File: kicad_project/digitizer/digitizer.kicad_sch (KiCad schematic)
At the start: 0 parts

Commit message: finished schematic symbol for the LPC1813JBD144, and connected it to the LQFP144 footprint! Placed it into the schematic
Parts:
- added U?: LPC1813JBD144, 495-project-library:LQFP-144_20x20mm_P0.5mm, symbol 495-project-library:LPC1813JBD144
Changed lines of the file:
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@@
 (kicad_sch (version 20211123) (generator eeschema)
   (paper "A4")
+  (symbol (lib_id "495-project-library:LPC1813JBD144") (at 240.03 142.24 90) (unit 1)
+    (in_bom yes) (on_board yes) (fields_autoplaced)
+    (property "Reference" "U?" (id 0) (at 248.92 22.1105 90))
+    (property "Value" "LPC1813JBD144" (id 1) (at 248.92 24.6505 90))
+    (property "Footprint" "495-project-library:LQFP-144_20x20mm_P0.5mm" (id 2) (at 99.695 67.31 0)
+      (effects (font (size 1.27 1.27)) hide)
+    )
+    (property "Datasheet" "" (id 3) (at 99.695 67.31 0)
+      (effects (font (size 1.27 1.27)) hide)
+    )
+    (pin "1")
+    (pin "10")
+    (pin "100")
+    (pin "101")
+    (pin "102")
+    (pin "103")
+    (pin "104")
+    (pin "105")
+    (pin "106")
+    (pin "107")
+    (pin "108")
+    (pin "109")
+    (pin "11")
+    (pin "110")
+    (pin "111")
+    (pin "112")
+    (pin "113")
+    (pin "114")
+    (pin "115")
+    (pin "116")
+    (pin "117")
+    (pin "118")
+    (pin "119")
+    (pin "12")
+    (pin "120")
+    (pin "121")
+    (pin "122")
+    (pin "123")
+    (pin "124")
+    (pin "125")
+    (pin "126")
+    (pin "127")
+    (pin "128")
+    (pin "129")
+    (pin "13")
+    (pin "130")
+    (pin "131")
+    (pin "132")
+    (pin "133")
+    (pin "134")
+    (pin "135")
+    (pin "136")
+    (pin "137")
+    (pin "138")
+    (pin "139")
+    (pin "14")
+    (pin "140")
+    (pin "141")
+    (pin "142")
+    (pin "143")
+    (pin "144")
+    (pin "15")
+    (pin "16")
+    (pin "17")
+    (pin "18")
+    (pin "19")
+    (pin "2")
+    (pin "20")
+    (pin "21")
+    (pin "22")
+    (pin "23")
+    (pin "24")
+    (pin "25")
+    (pin "26")
+    (pin "27")
+    (pin "28")
+    (pin "29")
+    (pin "3")
+    (pin "30")
+    (pin "31")
+    (pin "32")
+    (pin "33")
+    (pin "34")
+    (pin "35")
+    (pin "36")
+    (pin "37")
+    (pin "38")
+    (pin "39")
+    (pin "4")
+    (pin "40")
+    (pin "41")
+    (pin "42")
+    (pin "43")
+    (pin "44")
+    (pin "45")
+    (pin "46")
+    (pin "47")
+    (pin "48")
+    (pin "49")
+    (pin "5")
+    (pin "50")
+    (pin "51")
+    (pin "52")
+    (pin "53")
+    (pin "54")
+    (pin "55")
+    (pin "56")
+    (pin "57")
+    (pin "58")
+    (pin "59")
+    (pin "6")
+    (pin "60")
+    (pin "61")
+    (pin "62")
+    (pin "63")
+    (pin "64")
+    (pin "65")
+    (pin "66")
+    (pin "67")
+    (pin "68")
+    (pin "69")
+    (pin "7")
+    (pin "70")
+    (pin "71")
+    (pin "72")
+    (pin "73")
+    (pin "74")
+    (pin "75")
+    (pin "76")
+    (pin "77")
+    (pin "78")
+    (pin "79")
+    (pin "8")
+    (pin "80")
+    (pin "81")
+    (pin "82")
+    (pin "83")
+    (pin "84")
+    (pin "85")
+    (pin "86")
+    (pin "87")
+    (pin "88")
+    (pin "89")
+    (pin "9")
+    (pin "90")
+    (pin "91")
+    (pin "92")
+    (pin "93")
+    (pin "94")
+    (pin "95")
+    (pin "96")
+    (pin "97")
+    (pin "98")
+    (pin "99")
+  )
   (sheet_instances
     (path "/" (page "1"))
   )
+  (symbol_instances
+    (path "/52eeadc6-ab00-4433-9657-3deb36d0623b"
+      (reference "U?") (unit 1) (value "LPC1813JBD144") (footprint "495-project-library:LQFP-144_20x20mm_P0.5mm")
+    )
+  )
 )

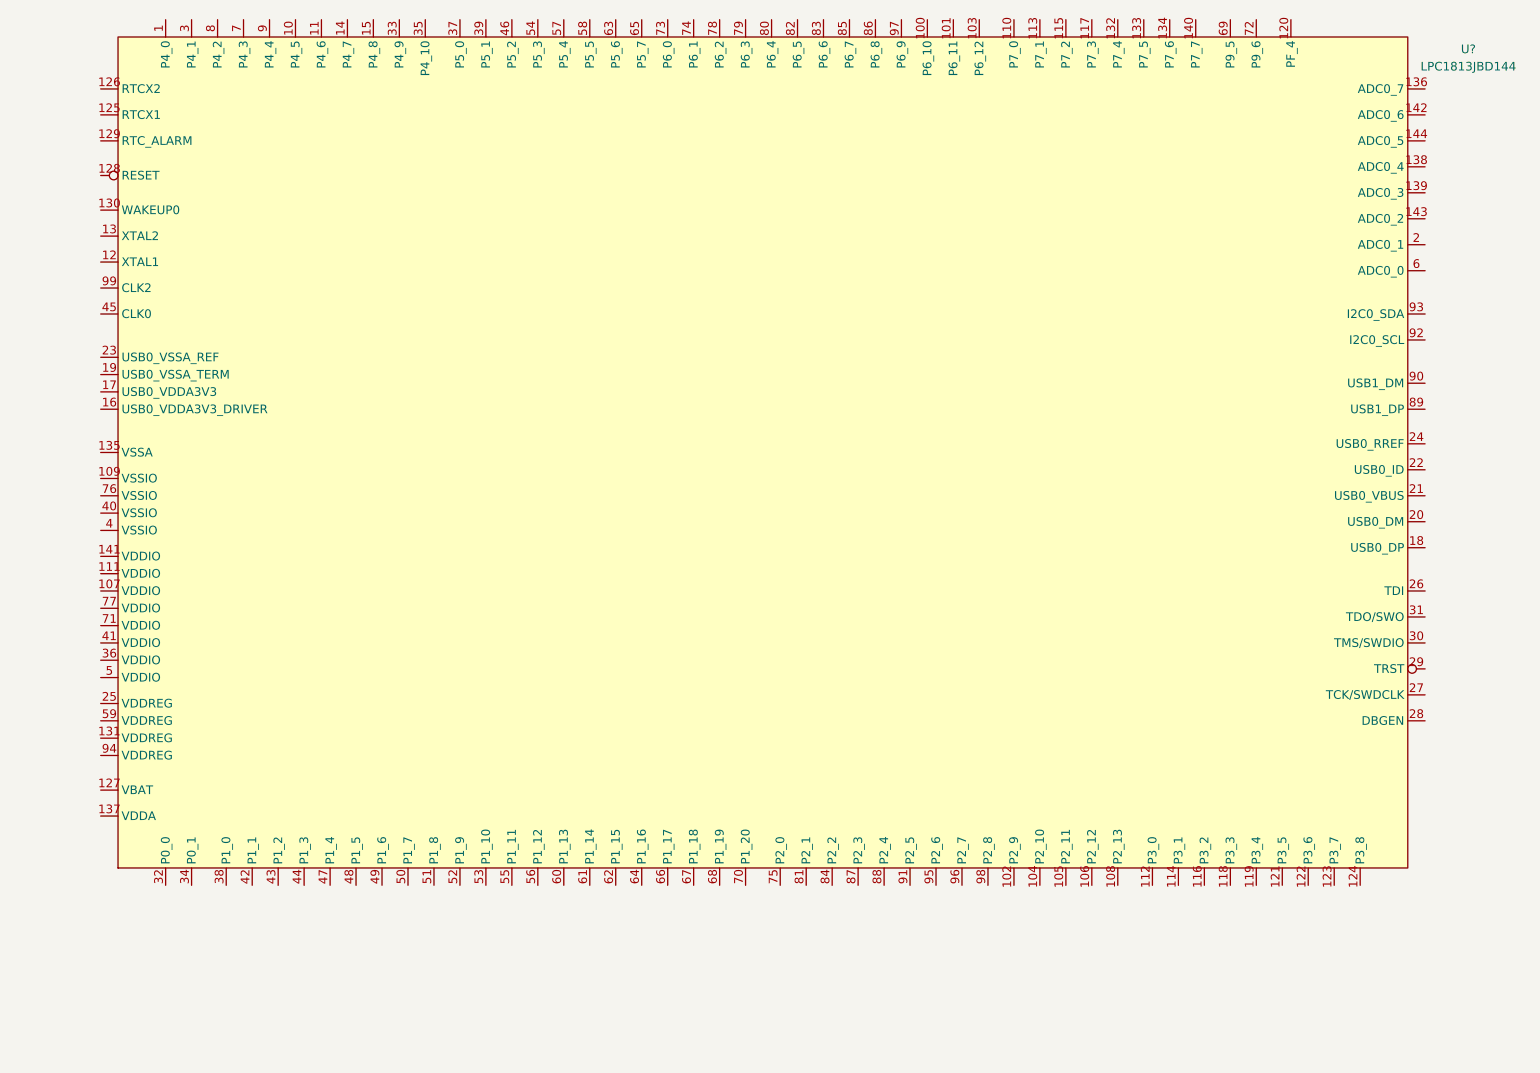
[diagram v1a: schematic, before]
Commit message: divided schematic up into 3 sheets, and placed the corresponding components within them. Have not connected anything or match the correct connectors to the proper footprints yet
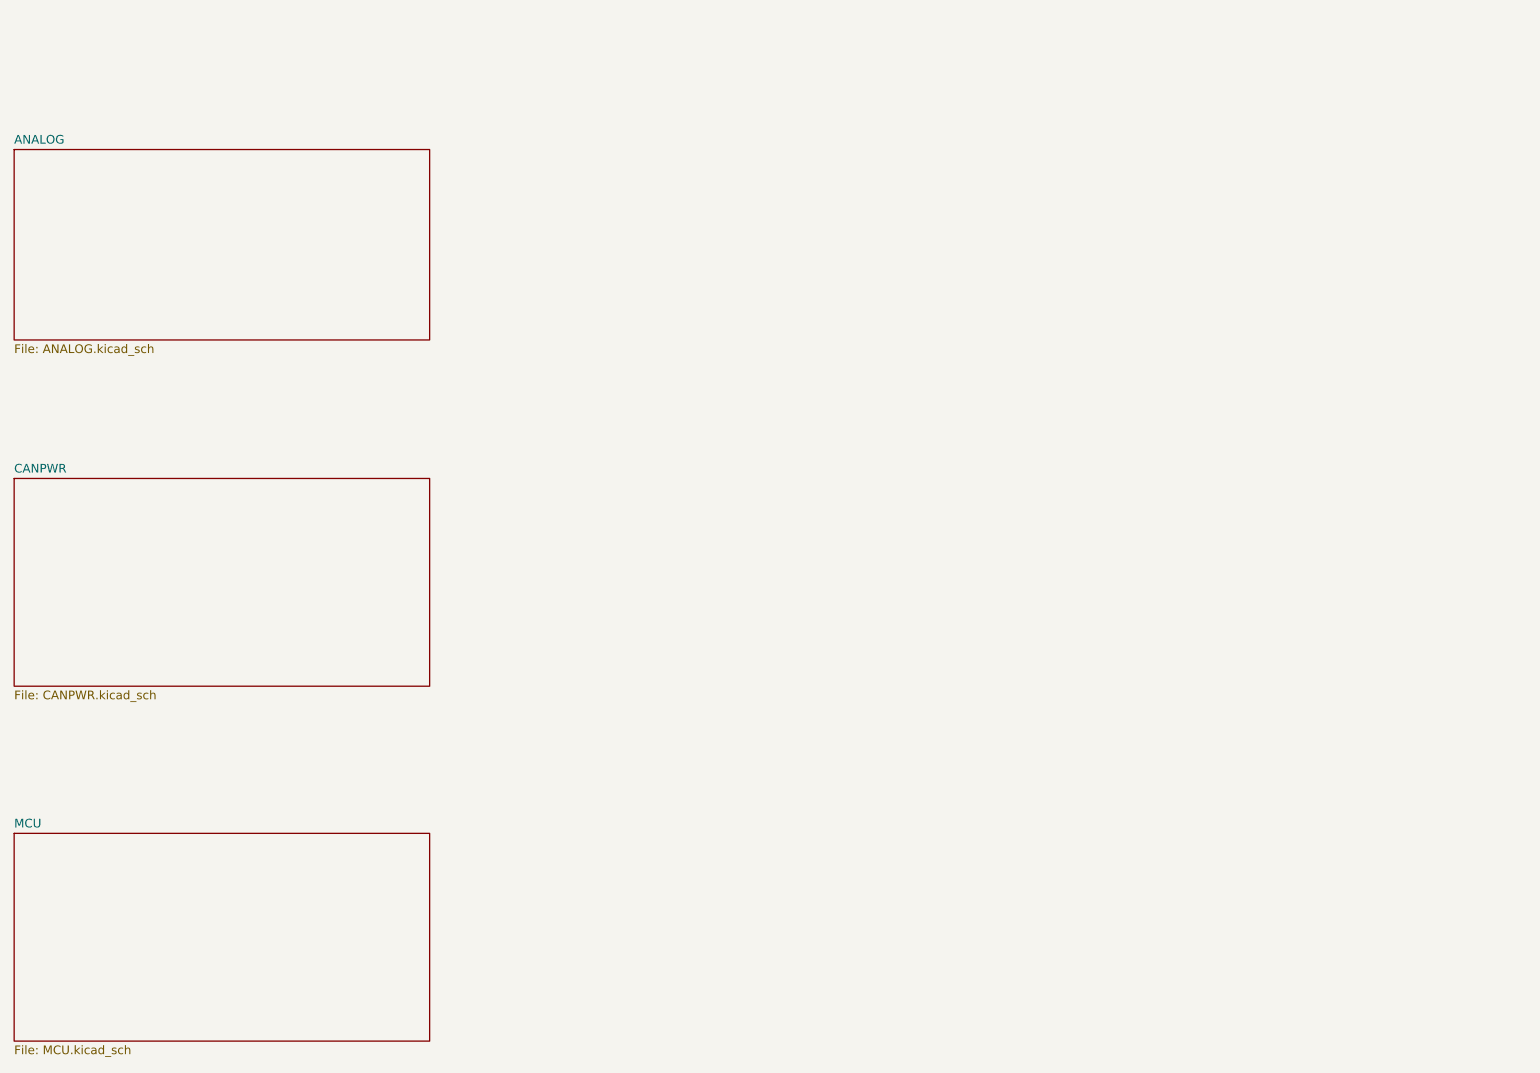
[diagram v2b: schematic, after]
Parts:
- removed U?: LPC1813JBD144, 495-project-library:LQFP-144_20x20mm_P0.5mm, symbol 495-project-library:LPC1813JBD144
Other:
- added sheet ANALOG (ANALOG.kicad_sch)
- added sheet CANPWR (CANPWR.kicad_sch)
- added sheet MCU (MCU.kicad_sch)
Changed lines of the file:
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@@
 (kicad_sch (version 20211123) (generator eeschema)
   (paper "A4")
-  (symbol (lib_id "495-project-library:LPC1813JBD144") (at 240.03 142.24 90) (unit 1)
-    (in_bom yes) (on_board yes) (fields_autoplaced)
-    (property "Reference" "U?" (id 0) (at 248.92 22.1105 90))
-    (property "Value" "LPC1813JBD144" (id 1) (at 248.92 24.6505 90))
-    (property "Footprint" "495-project-library:LQFP-144_20x20mm_P0.5mm" (id 2) (at 99.695 67.31 0)
-      (effects (font (size 1.27 1.27)) hide)
+  (sheet (at 35.56 137.16) (size 60.96 30.48) (fields_autoplaced)
+    (stroke (width 0.1524) (type solid) (color 0 0 0 0))
+    (fill (color 0 0 0 0.0000))
+    (property "Sheet name" "MCU" (id 0) (at 35.56 136.4484 0)
+      (effects (font (size 1.27 1.27)) (justify left bottom))
     )
-    (property "Datasheet" "" (id 3) (at 99.695 67.31 0)
-      (effects (font (size 1.27 1.27)) hide)
+    (property "Sheet file" "MCU.kicad_sch" (id 1) (at 35.56 168.2246 0)
+      (effects (font (size 1.27 1.27)) (justify left top))
     )
-    (pin "1")
-    (pin "10")
-    (pin "100")
-    (pin "101")
-    (pin "102")
-    (pin "103")
-    (pin "104")
-    (pin "105")
-    (pin "106")
-    (pin "107")
-    (pin "108")
-    (pin "109")
-    (pin "11")
-    (pin "110")
-    (pin "111")
-    (pin "112")
-    (pin "113")
-    (pin "114")
-    (pin "115")
-    (pin "116")
-    (pin "117")
-    (pin "118")
-    (pin "119")
-    (pin "12")
-    (pin "120")
-    (pin "121")
-    (pin "122")
-    (pin "123")
-    (pin "124")
-    (pin "125")
-    (pin "126")
-    (pin "127")
-    (pin "128")
-    (pin "129")
-    (pin "13")
-    (pin "130")
-    (pin "131")
-    (pin "132")
-    (pin "133")
-    (pin "134")
-    (pin "135")
-    (pin "136")
-    (pin "137")
-    (pin "138")
-    (pin "139")
-    (pin "14")
-    (pin "140")
-    (pin "141")
-    (pin "142")
-    (pin "143")
-    (pin "144")
-    (pin "15")
-    (pin "16")
-    (pin "17")
-    (pin "18")
-    (pin "19")
-    (pin "2")
-    (pin "20")
-    (pin "21")
-    (pin "22")
-    (pin "23")
-    (pin "24")
-    (pin "25")
-    (pin "26")
-    (pin "27")
-    (pin "28")
-    (pin "29")
-    (pin "3")
-    (pin "30")
-    (pin "31")
-    (pin "32")
-    (pin "33")
-    (pin "34")
-    (pin "35")
-    (pin "36")
-    (pin "37")
-    (pin "38")
-    (pin "39")
-    (pin "4")
-    (pin "40")
-    (pin "41")
-    (pin "42")
-    (pin "43")
-    (pin "44")
-    (pin "45")
-    (pin "46")
-    (pin "47")
-    (pin "48")
-    (pin "49")
-    (pin "5")
-    (pin "50")
-    (pin "51")
-    (pin "52")
-    (pin "53")
-    (pin "54")
-    (pin "55")
-    (pin "56")
-    (pin "57")
-    (pin "58")
-    (pin "59")
-    (pin "6")
-    (pin "60")
-    (pin "61")
-    (pin "62")
-    (pin "63")
-    (pin "64")
-    (pin "65")
-    (pin "66")
-    (pin "67")
-    (pin "68")
-    (pin "69")
-    (pin "7")
-    (pin "70")
-    (pin "71")
-    (pin "72")
-    (pin "73")
-    (pin "74")
-    (pin "75")
-    (pin "76")
-    (pin "77")
-    (pin "78")
-    (pin "79")
-    (pin "8")
-    (pin "80")
-    (pin "81")
-    (pin "82")
-    (pin "83")
-    (pin "84")
-    (pin "85")
-    (pin "86")
-    (pin "87")
-    (pin "88")
-    (pin "89")
-    (pin "9")
-    (pin "90")
-    (pin "91")
-    (pin "92")
-    (pin "93")
-    (pin "94")
-    (pin "95")
-    (pin "96")
-    (pin "97")
-    (pin "98")
-    (pin "99")
+  )
+  (sheet (at 35.56 36.83) (size 60.96 27.94) (fields_autoplaced)
+    (stroke (width 0.1524) (type solid) (color 0 0 0 0))
+    (fill (color 0 0 0 0.0000))
+    (property "Sheet name" "ANALOG" (id 0) (at 35.56 36.1184 0)
+      (effects (font (size 1.27 1.27)) (justify left bottom))
+    )
+    (property "Sheet file" "ANALOG.kicad_sch" (id 1) (at 35.56 65.3546 0)
+      (effects (font (size 1.27 1.27)) (justify left top))
+    )
+  )
+  (sheet (at 35.56 85.09) (size 60.96 30.48) (fields_autoplaced)
+    (stroke (width 0.1524) (type solid) (color 0 0 0 0))
+    (fill (color 0 0 0 0.0000))
+    (property "Sheet name" "CANPWR" (id 0) (at 35.56 84.3784 0)
+      (effects (font (size 1.27 1.27)) (justify left bottom))
+    )
+    (property "Sheet file" "CANPWR.kicad_sch" (id 1) (at 35.56 116.1546 0)
+      (effects (font (size 1.27 1.27)) (justify left top))
+    )
   )
   (sheet_instances
     (path "/" (page "1"))
+    (path "/e2c8983e-9459-4573-b339-1f4298bf65be" (page "3"))
+    (path "/8e4bebbd-b918-44d5-8394-c191f4e972d3" (page "4"))
+    (path "/59857acb-489d-4d58-af14-88362a204248" (page "4"))
   )
   (symbol_instances
-    (path "/52eeadc6-ab00-4433-9657-3deb36d0623b"
+    (path "/e2c8983e-9459-4573-b339-1f4298bf65be/3e420adc-3f3e-4ad7-b9e2-5ff4f66087d2"
+      (reference "IC?") (unit 1) (value "MAX6035AAUR50+T") (footprint "SOT95P237X112-3N")
+    )
+    (path "/59857acb-489d-4d58-af14-88362a204248/435a8de2-d92d-404b-a204-1b8d6d9f362a"
+      (reference "IC?") (unit 1) (value "MAX3059ASA+T") (footprint "SOIC127P600X175-8N")
+    )
+    (path "/8e4bebbd-b918-44d5-8394-c191f4e972d3/5b20aef5-6bd8-47f7-86aa-1a7e55b9d139"
+      (reference "IC?") (unit 1) (value "ADS1234IPWR") (footprint "SOP65P640X120-28N")
+    )
+    (path "/59857acb-489d-4d58-af14-88362a204248/84e94675-43a7-4212-9e62-0f780abfd06b"
+      (reference "IC?") (unit 1) (value "MAX3059ASA+T") (footprint "SOIC127P600X175-8N")
+    )
+    (path "/e2c8983e-9459-4573-b339-1f4298bf65be/932b1a92-f5d2-47d1-b1f0-1f4180d05597"
+      (reference "IC?") (unit 1) (value "MAX6043BAUT33+T") (footprint "SOT95P280X145-6N")
+    )
+    (path "/8e4bebbd-b918-44d5-8394-c191f4e972d3/2d66c624-9968-40cd-9f77-7c3c08aebcc4"
+      (reference "J?") (unit 1) (value "Conn_01x04_Shielded") (footprint "")
+    )
+    (path "/59857acb-489d-4d58-af14-88362a204248/4fddafb8-a80f-479c-bb72-09844a9cb710"
+      (reference "J?") (unit 1) (value "Conn_02x05_Odd_Even") (footprint "")
+    )
+    (path "/8e4bebbd-b918-44d5-8394-c191f4e972d3/5869e0e4-d092-4d61-b78f-cfb0c7b24996"
+      (reference "J?") (unit 1) (value "Conn_01x04_Shielded") (footprint "")
+    )
+    (path "/8e4bebbd-b918-44d5-8394-c191f4e972d3/6a83202a-13be-499d-b6b6-ad5d3d904d4f"
+      (reference "J?") (unit 1) (value "Conn_01x04_Shielded") (footprint "")
+    )
+    (path "/e2c8983e-9459-4573-b339-1f4298bf65be/b0aa02d7-c635-47f3-95a7-51b0d8bfd025"
+      (reference "J?") (unit 1) (value "Conn_02x02_Top_Bottom") (footprint "")
+    )
+    (path "/e2c8983e-9459-4573-b339-1f4298bf65be/cb564194-f3a5-43dc-92c5-a4986c563991"
+      (reference "J?") (unit 1) (value "Conn_02x02_Top_Bottom") (footprint "")
+    )
+    (path "/59857acb-489d-4d58-af14-88362a204248/5d6dce58-c829-40b0-b42d-4480008ea013"
       (reference "U?") (unit 1) (value "LPC1813JBD144") (footprint "495-project-library:LQFP-144_20x20mm_P0.5mm")
     )
